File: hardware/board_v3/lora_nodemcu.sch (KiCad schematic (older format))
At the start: 48 parts, among them J1 Solar Panel, J2 LiPo 18650, J3 RESET_BUTTON, J4 ESP_PRGM, J5 RGB_LED, J6 RF_Shield_ESP-07S, J7 RF_Shield_RFM95, Q1 2N3904, Q2 2N3904, Q3 2N3904, SW1 SW_SPST, U1 CN3791_module, U2 ESP-07S, U3 LM1117-3.3, U4 RFM95

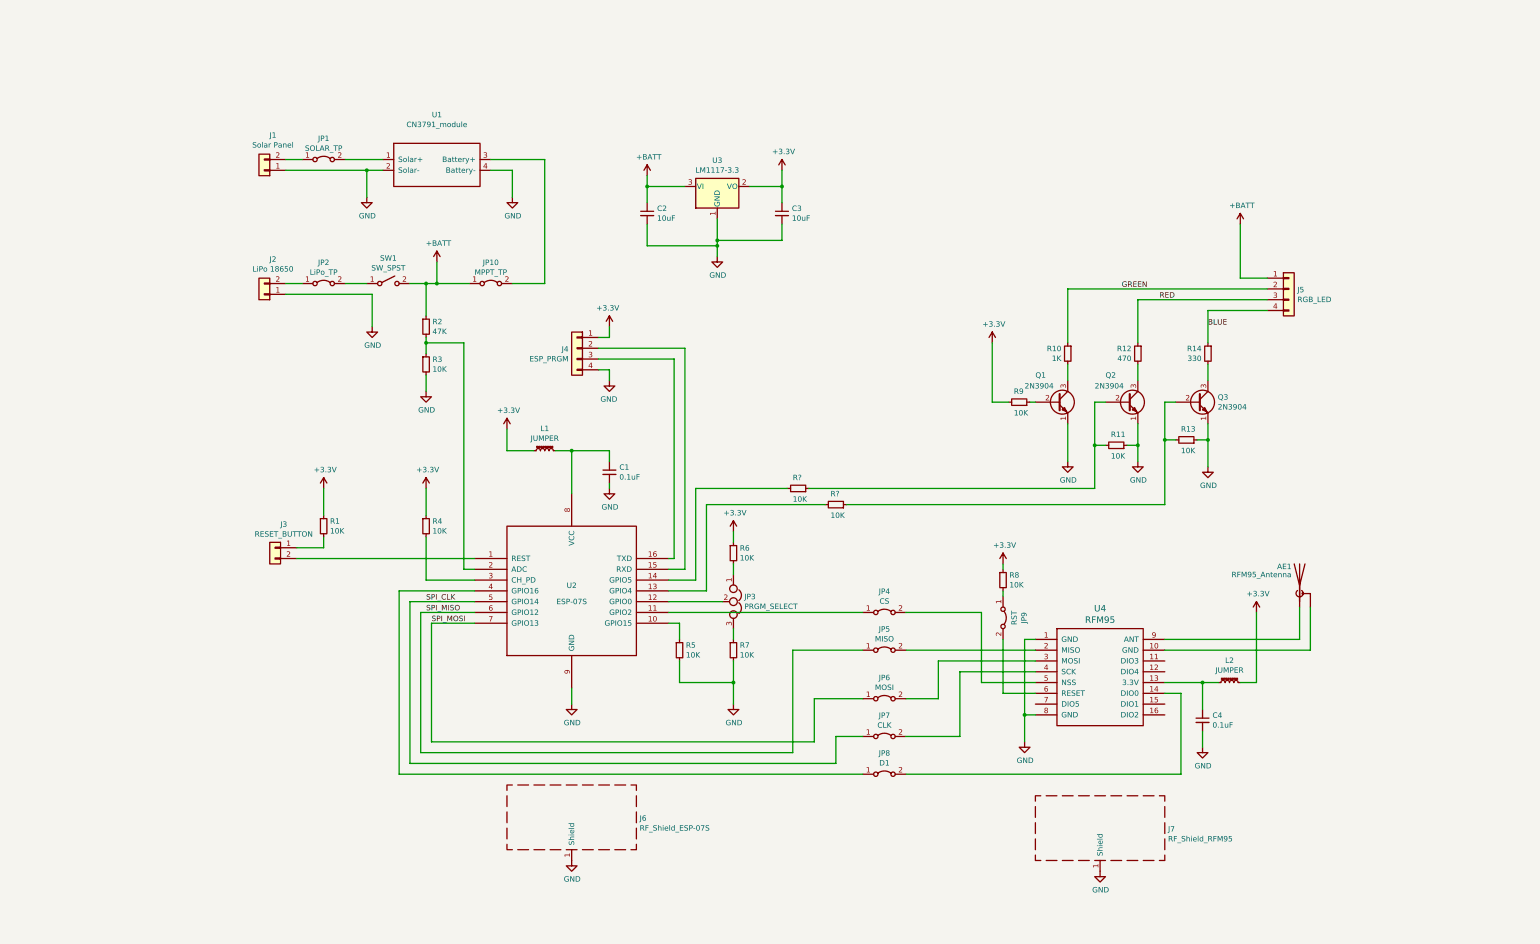
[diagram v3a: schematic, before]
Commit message: completes layout of board with most 3d shapes
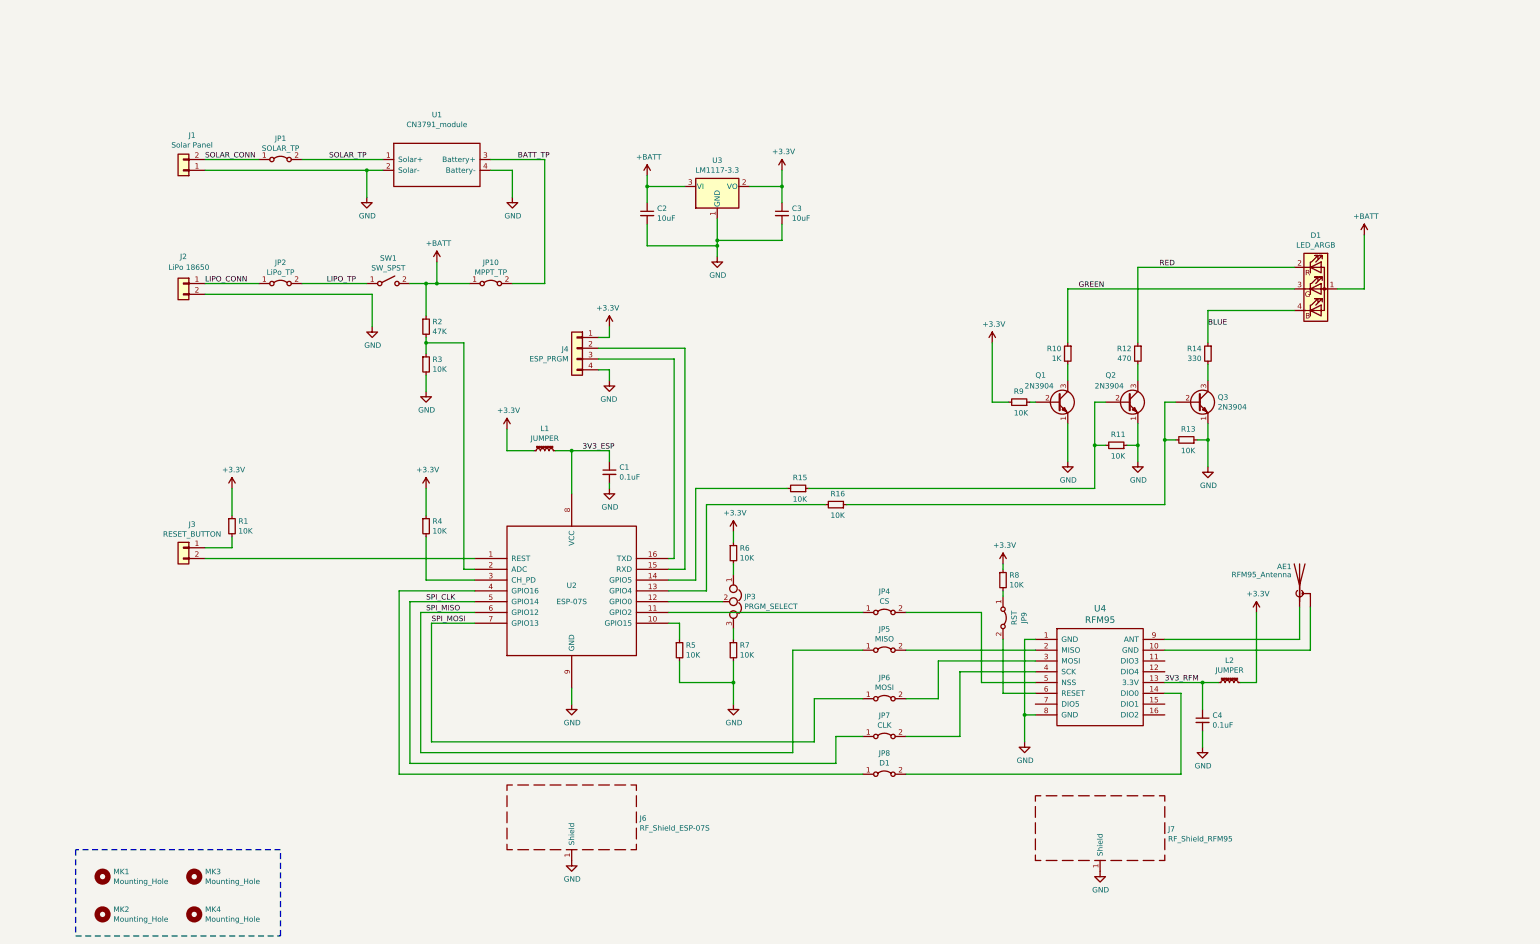
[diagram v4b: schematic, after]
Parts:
- removed J5: RGB_LED, Connector_Phoenix_MC:PhoenixContact_MCV_1,5_4-G-5.08_1x04_P5.08mm_Vertical, symbol Connector_Generic:Conn_01x04
- added D1: LED_ARGB, LED_THT:LED_D5.0mm-4, symbol Device:LED_ARGB
- added MK1, MK2, MK3, MK4: Mounting_Hole, MountingHole:MountingHole_3.2mm_M3, symbol Mechanical:Mounting_Hole
- J1: footprint Connector_Phoenix_MC:PhoenixContact_MCV_1,5_2-G-5.08_1x02_P5.08mm_Vertical -> disaster_radio:solar_panel_conn
- gave numbers to parts that had none: 2
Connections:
- net +BATT: now also D1.1 (A)
- net BLUE: now also D1.4 (BK)
- net GND: now also J2.2 (Pin_2); no longer J2.1 (Pin_1)
- net GREEN: now also D1.3 (GK)
- net RED: now also D1.2 (RK)
- net 3V3_ESP: now reaches C1.1, L1.2, U2.8 (VCC)
- net 3V3_RFM: now reaches C4.1, L2.1, U4.13 (3.3V)
- net LIPO_CONN: now reaches JP2.1 (A)
- net LIPO_CONN: now also J2.1 (Pin_1); no longer J2.2 (Pin_2)
- net SOLAR_CONN: now reaches J1.2 (Pin_2), JP1.1 (A)
- net SOLAR_TP: now reaches JP1.2 (B), U1.1 (Solar+)
- net BATT_TP: now reaches JP10.2 (B), U1.3 (Battery+)
- net LIPO_TP: now reaches JP2.2 (B), SW1.1 (A)
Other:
- moved on the sheet: J1, J2, J3, JP1, JP2, R1
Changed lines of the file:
@@
 L Connector_Generic:Conn_01x02 J2
 U 1 1 5AA4CAA2
-P 3350 3550
-F 0 "J2" H 3270 3225 50  0000 C CNN
-F 1 "LiPo 18650" H 3270 3316 50  0000 C CNN
-F 2 "Battery:BatteryHolder_MPD_BH-18650-PC2" H 3350 3550 50  0001 C CNN
-F 3 "~" H 3350 3550 50  0001 C CNN
-	1    3350 3550
-	-1   0    0    1
+P 2600 3450
+F 0 "J2" H 2600 3700 50  0000 C CNN
+F 1 "LiPo 18650" H 2550 3600 50  0000 C CNN
+F 2 "Battery:BatteryHolder_MPD_BH-18650-PC2" H 2600 3450 50  0001 C CNN
+F 3 "~" H 2600 3450 50  0001 C CNN
+	1    2600 3450
+	-1   0    0    -1
 $EndComp
 $Comp
@@
 L Connector_Generic:Conn_01x02 J1
 U 1 1 5AA4DEE1
-P 3350 2400
-F 0 "J1" H 3270 2075 50  0000 C CNN
-F 1 "Solar Panel" H 3270 2166 50  0000 C CNN
-F 2 "Connector_Phoenix_MC:PhoenixContact_MCV_1,5_2-G-5.08_1x02_P5.08mm_Vertical" H 3350 2400 50  0001 C CNN
-F 3 "~" H 3350 2400 50  0001 C CNN
-	1    3350 2400
+P 2600 2400
+F 0 "J1" H 2520 2075 50  0000 C CNN
+F 1 "Solar Panel" H 2520 2166 50  0000 C CNN
+F 2 "disaster_radio:solar_panel_conn" H 2600 2400 50  0001 C CNN
+F 3 "~" H 2600 2400 50  0001 C CNN
+	1    2600 2400
 	-1   0    0    1
 $EndComp
@@
 	4300 2650 4300 2400
 Wire Wire Line
-	4300 2400 3550 2400
+	4300 2400 2800 2400
 Wire Wire Line
 	4300 2400 4450 2400
@@
 	4350 3850 4350 3550
 Wire Wire Line
-	4350 3550 3550 3550
+	4350 3550 2800 3550
 Wire Wire Line
 	4950 3250 4950 3450
@@
 L Connector_Generic:Conn_01x02 J3
 U 1 1 5AAC3057
-P 3450 5900
-F 0 "J3" H 3370 6117 50  0000 C CNN
-F 1 "RESET_BUTTON" H 3370 6026 50  0000 C CNN
-F 2 "Connector_Phoenix_MC:PhoenixContact_MCV_1,5_2-G-5.08_1x02_P5.08mm_Vertical" H 3450 5900 50  0001 C CNN
-F 3 "~" H 3450 5900 50  0001 C CNN
-	1    3450 5900
+P 2600 5900
+F 0 "J3" H 2520 6117 50  0000 C CNN
+F 1 "RESET_BUTTON" H 2520 6026 50  0000 C CNN
+F 2 "Connector_Phoenix_MC:PhoenixContact_MCV_1,5_2-G-5.08_1x02_P5.08mm_Vertical" H 2600 5900 50  0001 C CNN
+F 3 "~" H 2600 5900 50  0001 C CNN
+	1    2600 5900
 	-1   0    0    -1
 $EndComp
 Wire Wire Line
-	3650 6000 5300 6000
+	2800 6000 5300 6000
 $Comp
 L Device:R_Small R1
 U 1 1 5AACACF4
-P 3900 5700
-F 0 "R1" H 3959 5746 50  0000 L CNN
-F 1 "10K" H 3959 5655 50  0000 L CNN
-F 2 "Resistor_SMD:R_0805_2012Metric_Pad1.15x1.50mm_HandSolder" H 3900 5700 50  0001 C CNN
-F 3 "~" H 3900 5700 50  0001 C CNN
-	1    3900 5700
+P 3050 5700
+F 0 "R1" H 3109 5746 50  0000 L CNN
+F 1 "10K" H 3109 5655 50  0000 L CNN
+F 2 "Resistor_SMD:R_0805_2012Metric_Pad1.15x1.50mm_HandSolder" H 3050 5700 50  0001 C CNN
+F 3 "~" H 3050 5700 50  0001 C CNN
+	1    3050 5700
 	1    0    0    -1
 $EndComp
@@
 L lora_nodemcu-cache:+3.3V #PWR0114
 U 1 1 5AACADA4
-P 3900 5350
-F 0 "#PWR0114" H 3900 5200 50  0001 C CNN
-F 1 "+3.3V" H 3915 5523 50  0000 C CNN
-F 2 "" H 3900 5350 50  0001 C CNN
-F 3 "" H 3900 5350 50  0001 C CNN
-	1    3900 5350
+P 3050 5350
+F 0 "#PWR0114" H 3050 5200 50  0001 C CNN
+F 1 "+3.3V" H 3065 5523 50  0000 C CNN
+F 2 "" H 3050 5350 50  0001 C CNN
+F 3 "" H 3050 5350 50  0001 C CNN
+	1    3050 5350
 	1    0    0    -1
 $EndComp
@@
 	4850 5350 4850 5600
 Wire Wire Line
-	3900 5350 3900 5600
-Wire Wire Line
-	3900 5800 3900 5900
-Wire Wire Line
-	3900 5900 3650 5900
+	3050 5350 3050 5600
+Wire Wire Line
+	3050 5800 3050 5900
+Wire Wire Line
+	3050 5900 2800 5900
 $Comp
 L Device:R_Small R7
@@
 Wire Wire Line
 	13050 6850 11700 6850
-$Comp
-L Connector_Generic:Conn_01x04 J5
-U 1 1 5AB95801
-P 12850 3500
-F 0 "J5" H 12929 3492 50  0000 L CNN
-F 1 "RGB_LED" H 12929 3401 50  0000 L CNN
-F 2 "Connector_Phoenix_MC:PhoenixContact_MCV_1,5_4-G-5.08_1x04_P5.08mm_Vertical" H 12850 3500 50  0001 C CNN
-F 3 "~" H 12850 3500 50  0001 C CNN
-	1    12850 3500
-	1    0    0    -1
-$EndComp
 Wire Wire Line
 	4900 6600 4900 7700
@@
 L Jumper:Jumper_2_Bridged JP1
 U 1 1 5AAA022A
-P 3900 2300
-F 0 "JP1" H 3900 2495 50  0000 C CNN
-F 1 "SOLAR_TP" H 3900 2404 50  0000 C CNN
-F 2 "Jumper:SolderJumper-2_P1.3mm_Bridged_Pad1.0x1.5mm" H 3900 2300 50  0001 C CNN
-F 3 "~" H 3900 2300 50  0001 C CNN
-	1    3900 2300
+P 3500 2300
+F 0 "JP1" H 3500 2495 50  0000 C CNN
+F 1 "SOLAR_TP" H 3500 2404 50  0000 C CNN
+F 2 "Jumper:SolderJumper-2_P1.3mm_Bridged_Pad1.0x1.5mm" H 3500 2300 50  0001 C CNN
+F 3 "~" H 3500 2300 50  0001 C CNN
+	1    3500 2300
 	1    0    0    -1
 $EndComp
@@
 L Jumper:Jumper_2_Bridged JP2
 U 1 1 5AAA0488
-P 3900 3450
-F 0 "JP2" H 3900 3645 50  0000 C CNN
-F 1 "LiPo_TP" H 3900 3554 50  0000 C CNN
-F 2 "Jumper:SolderJumper-2_P1.3mm_Bridged_Pad1.0x1.5mm" H 3900 3450 50  0001 C CNN
-F 3 "~" H 3900 3450 50  0001 C CNN
-	1    3900 3450
-	1    0    0    -1
-$EndComp
-Wire Wire Line
-	4100 3450 4300 3450
-Wire Wire Line
-	3700 3450 3550 3450
-Wire Wire Line
-	4100 2300 4450 2300
-Wire Wire Line
-	3700 2300 3550 2300
+P 3500 3450
+F 0 "JP2" H 3500 3645 50  0000 C CNN
+F 1 "LiPo_TP" H 3500 3554 50  0000 C CNN
+F 2 "Jumper:SolderJumper-2_P1.3mm_Bridged_Pad1.0x1.5mm" H 3500 3450 50  0001 C CNN
+F 3 "~" H 3500 3450 50  0001 C CNN
+	1    3500 3450
+	1    0    0    -1
+$EndComp
+Wire Wire Line
+	3700 3450 4300 3450
+Wire Wire Line
+	3300 3450 2800 3450
+Wire Wire Line
+	3700 2300 4450 2300
+Wire Wire Line
+	3300 2300 2800 2300
 $Comp
 L Device:R_Small R3
@@
 $EndComp
 Wire Wire Line
-	12650 3700 12100 3700
-Wire Wire Line
 	12100 3700 12100 4000
 Wire Wire Line
-	12650 3600 11450 3600
-Wire Wire Line
-	11450 3600 11450 4000
-Wire Wire Line
-	12650 3500 10800 3500
+	11450 3300 11450 4000
 Wire Wire Line
 	10800 3500 10800 4000
@@
 Wire Wire Line
 	11450 4950 11450 5100
-Text Label 11300 3500 0    50   ~ 0
+Text Label 10900 3500 0    50   ~ 0
 GREEN
-Text Label 11650 3600 0    50   ~ 0
+Text Label 11650 3300 0    50   ~ 0
 RED
 Text Label 12100 3850 0    50   ~ 0
@@
 L power:+BATT #PWR0125
 U 1 1 5ADE71D1
-P 12400 2900
-F 0 "#PWR0125" H 12400 2750 50  0001 C CNN
-F 1 "+BATT" H 12415 3073 50  0000 C CNN
-F 2 "" H 12400 2900 50  0001 C CNN
-F 3 "" H 12400 2900 50  0001 C CNN
-	1    12400 2900
-	1    0    0    -1
-$EndComp
-Wire Wire Line
-	12400 2900 12400 3400
-Wire Wire Line
-	12400 3400 12650 3400
+P 13550 3000
+F 0 "#PWR0125" H 13550 2850 50  0001 C CNN
+F 1 "+BATT" H 13565 3173 50  0000 C CNN
+F 2 "" H 13550 3000 50  0001 C CNN
+F 3 "" H 13550 3000 50  0001 C CNN
+	1    13550 3000
+	1    0    0    -1
+$EndComp
+Wire Wire Line
+	13550 3000 13550 3500
 $Comp
 L Device:R_Small R5
@@
 	5650 3450 5950 3450
 $Comp
-L Device:R_Small R?
+L Device:R_Small R15
 U 1 1 5AAECE0B
 P 8300 5350
-F 0 "R?" V 8400 5300 50  0000 L CNN
+F 0 "R15" V 8400 5300 50  0000 L CNN
 F 1 "10K" V 8200 5300 50  0000 L CNN
 F 2 "Resistor_SMD:R_0805_2012Metric_Pad1.15x1.50mm_HandSolder" H 8300 5350 50  0001 C CNN
@@
 $EndComp
 $Comp
-L Device:R_Small R?
+L Device:R_Small R16
 U 1 1 5AAED216
 P 8650 5500
-F 0 "R?" V 8750 5450 50  0000 L CNN
+F 0 "R16" V 8750 5450 50  0000 L CNN
 F 1 "10K" V 8550 5450 50  0000 L CNN
 F 2 "Resistor_SMD:R_0805_2012Metric_Pad1.15x1.50mm_HandSolder" H 8650 5500 50  0001 C CNN
@@
 Wire Wire Line
 	11700 5500 8750 5500
+$Comp
+L Mechanical:Mounting_Hole MK1
+U 1 1 5ABC6521
+P 1850 8950
+F 0 "MK1" H 1950 8996 50  0000 L CNN
+F 1 "Mounting_Hole" H 1950 8905 50  0000 L CNN
+F 2 "MountingHole:MountingHole_3.2mm_M3" H 1850 8950 50  0001 C CNN
+F 3 "" H 1850 8950 50  0001 C CNN
+	1    1850 8950
+	1    0    0    -1
+$EndComp
+$Comp
+L Mechanical:Mounting_Hole MK3
+U 1 1 5ABC68A6
+P 2700 8950
+F 0 "MK3" H 2800 8996 50  0000 L CNN
+F 1 "Mounting_Hole" H 2800 8905 50  0000 L CNN
+F 2 "MountingHole:MountingHole_3.2mm_M3" H 2700 8950 50  0001 C CNN
+F 3 "" H 2700 8950 50  0001 C CNN
+	1    2700 8950
+	1    0    0    -1
+$EndComp
+$Comp
+L Mechanical:Mounting_Hole MK2
+U 1 1 5ABC6A8E
+P 1850 9300
+F 0 "MK2" H 1950 9346 50  0000 L CNN
+F 1 "Mounting_Hole" H 1950 9255 50  0000 L CNN
+F 2 "MountingHole:MountingHole_3.2mm_M3" H 1850 9300 50  0001 C CNN
+F 3 "" H 1850 9300 50  0001 C CNN
+	1    1850 9300
+	1    0    0    -1
+$EndComp
+$Comp
+L Mechanical:Mounting_Hole MK4
+U 1 1 5ABC6A95
+P 2700 9300
+F 0 "MK4" H 2800 9346 50  0000 L CNN
+F 1 "Mounting_Hole" H 2800 9255 50  0000 L CNN
+F 2 "MountingHole:MountingHole_3.2mm_M3" H 2700 9300 50  0001 C CNN
+F 3 "" H 2700 9300 50  0001 C CNN
+	1    2700 9300
+	1    0    0    -1
+$EndComp
+$Comp
+L Device:LED_ARGB D1
+U 1 1 5ABCE072
+P 13100 3500
+F 0 "D1" H 13100 3997 50  0000 C CNN
+F 1 "LED_ARGB" H 13100 3906 50  0000 C CNN
+F 2 "LED_THT:LED_D5.0mm-4" H 13100 3450 50  0001 C CNN
+F 3 "~" H 13100 3450 50  0001 C CNN
+	1    13100 3500
+	1    0    0    -1
+$EndComp
+Wire Wire Line
+	13300 3500 13550 3500
+Wire Wire Line
+	11450 3300 12900 3300
+Wire Wire Line
+	10800 3500 12900 3500
+Wire Wire Line
+	12100 3700 12900 3700
+Wire Notes Line
+	1600 8700 1600 9500
+Wire Notes Line
+	1600 9500 3500 9500
+Wire Notes Line
+	3500 9500 3500 8700
+Wire Notes Line
+	3500 8700 1600 8700
+Text Label 5700 2300 0    50   ~ 0
+BATT_TP
+Text Label 4200 3450 2    50   ~ 0
+LIPO_TP
+Text Label 3950 2300 0    50   ~ 0
+SOLAR_TP
+Text Label 2800 2300 0    50   ~ 0
+SOLAR_CONN
+Text Label 2800 3450 0    50   ~ 0
+LIPO_CONN
+Text Label 6300 5000 0    50   ~ 0
+3V3_ESP
+Text Label 11700 7150 0    50   ~ 0
+3V3_RFM
 $EndSCHEMATC

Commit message: adds new ESP32 board
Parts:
- MK1, MK2, MK3, MK4: symbol Mechanical:Mounting_Hole -> lora_nodemcu-rescue:Mounting_Hole-Mechanical
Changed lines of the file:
@@
 EESchema Schematic File Version 4
 LIBS:lora_nodemcu-cache
-EELAYER 26 0
+EELAYER 29 0
 EELAYER END
 $Descr A3 16535 11693
@@
 	11700 5500 8750 5500
 $Comp
-L Mechanical:Mounting_Hole MK1
+L lora_nodemcu-rescue:Mounting_Hole-Mechanical MK1
 U 1 1 5ABC6521
 P 1850 8950
@@
 $EndComp
 $Comp
-L Mechanical:Mounting_Hole MK3
+L lora_nodemcu-rescue:Mounting_Hole-Mechanical MK3
 U 1 1 5ABC68A6
 P 2700 8950
@@
 $EndComp
 $Comp
-L Mechanical:Mounting_Hole MK2
+L lora_nodemcu-rescue:Mounting_Hole-Mechanical MK2
 U 1 1 5ABC6A8E
 P 1850 9300
@@
 $EndComp
 $Comp
-L Mechanical:Mounting_Hole MK4
+L lora_nodemcu-rescue:Mounting_Hole-Mechanical MK4
 U 1 1 5ABC6A95
 P 2700 9300
